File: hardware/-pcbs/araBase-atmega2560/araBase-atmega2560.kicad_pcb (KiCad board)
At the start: 2 copper layers, 21 parts, among them J1 UI, U1 ATmega2560-16AU, U2 5V->3.3V, Y1 16MHz

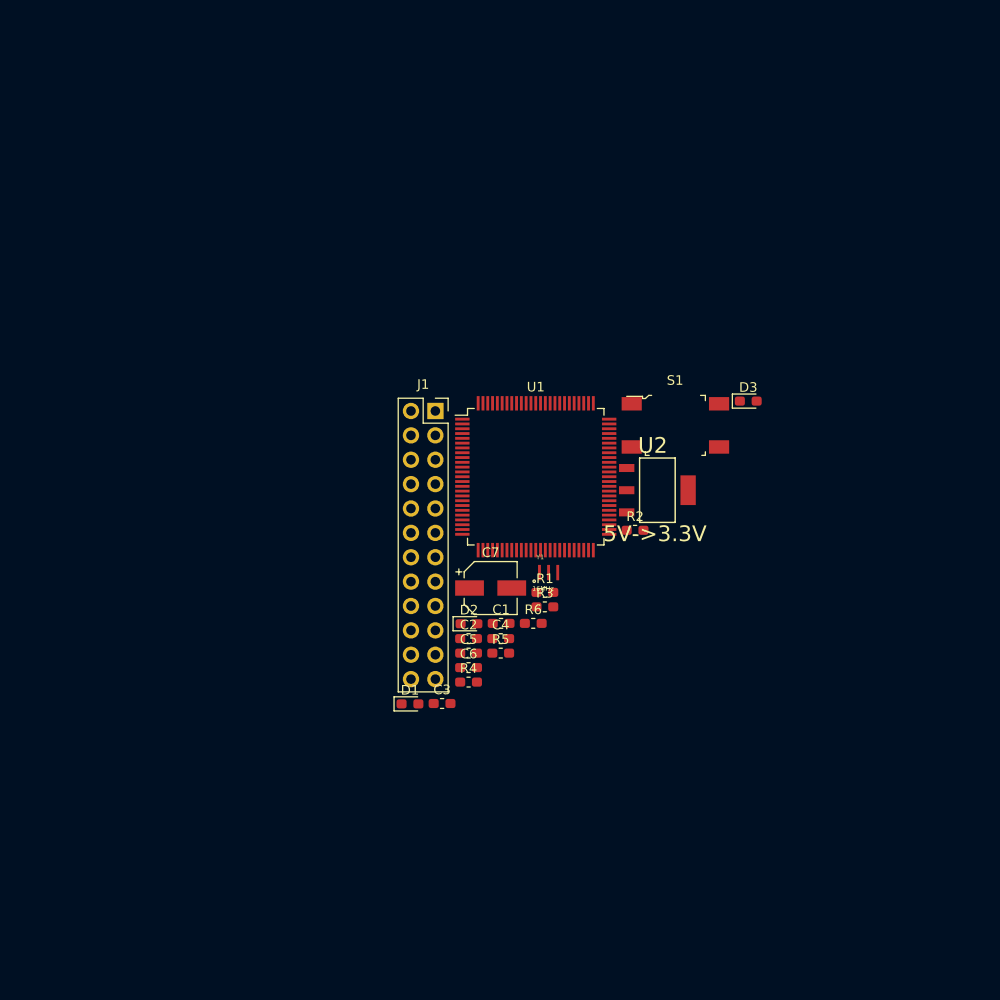
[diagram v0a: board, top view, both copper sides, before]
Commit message: Add 100mmx100mm edge cut and distribute footprints
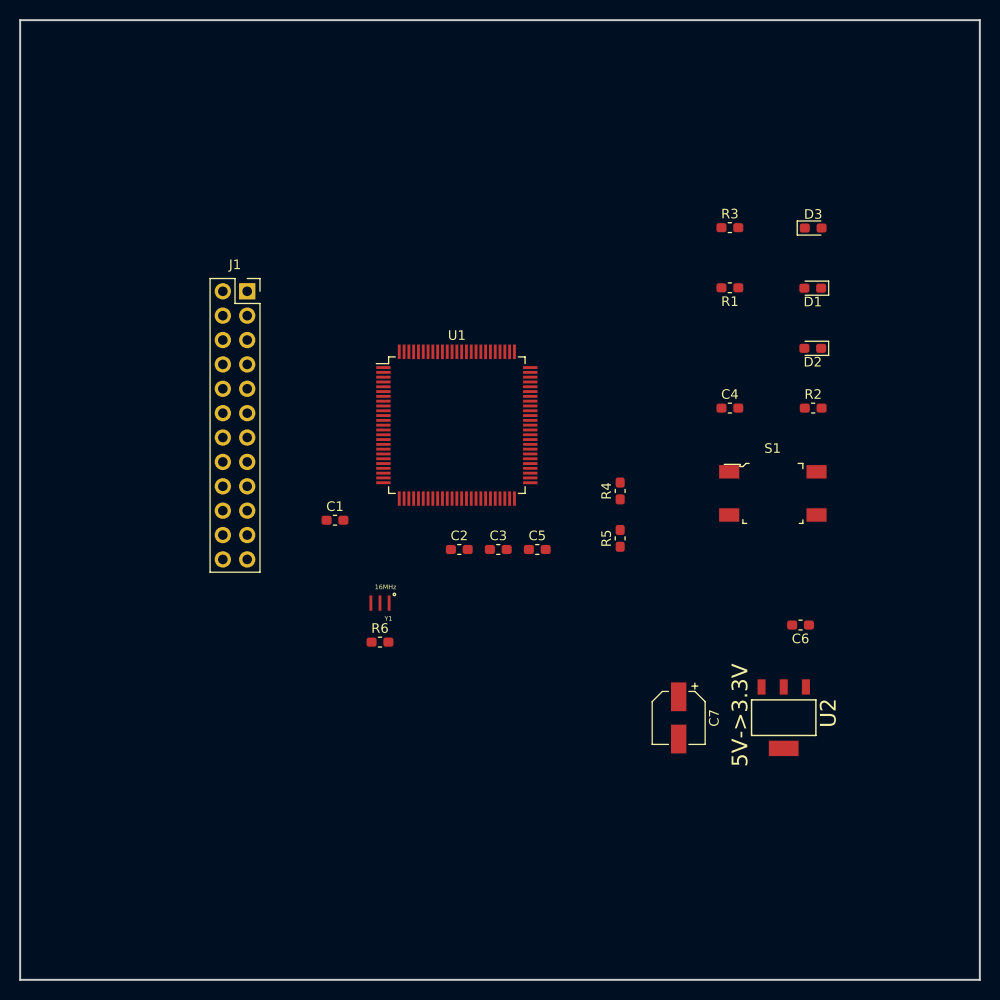
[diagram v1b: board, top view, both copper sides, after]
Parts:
- moved D1 60.3 mm to (132.6, 77.9), turned to 180 degrees
- moved D2 45.9 mm to (132.6, 84.2), turned to 180 degrees
- moved R3 44.0 mm to (124.0, 71.6)
- moved R1 37.1 mm to (124.0, 77.9), turned to 180 degrees
- moved C6 34.9 mm to (131.3, 113.0), turned to 180 degrees
- moved C4 33.9 mm to (124.0, 90.4)
- moved U2 27.1 mm to (129.6, 122.7), turned to 270 degrees
- moved R4 25.4 mm to (112.5, 99.1), turned to 90 degrees
- moved C7 23.8 mm to (118.6, 122.7), turned to 270 degrees
- moved J1 23.2 mm to (73.7, 78.3)
- moved R2 22.5 mm to (132.6, 90.4)
- moved C1 20.4 mm to (82.8, 102.1)
- moved D3 19.3 mm to (132.6, 71.7)
- moved Y1 17.9 mm to (87.5, 110.7), turned to 180 degrees
- moved R5 17.3 mm to (112.5, 104.0), turned to 90 degrees
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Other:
- board outline added: 100 x 100 mm

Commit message: Setup design rules for 10mil/10mil trace and 0.8mm/0.4mm via/drill
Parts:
- moved C2 3.09 mm to (92.7, 105.7), turned to 90 degrees
- moved C3 3.09 mm to (96.8, 105.7), turned to 90 degrees
- moved C5 3.09 mm to (100.8, 105.7), turned to 90 degrees
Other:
- net class Default: clearance 0.2 -> 0.254; trace_width 0.25 -> 0.254
- net class PWR added: clearance 0.3048, trace_width 0.3048, via_dia 0.8, via_drill 0.4
- rule trace_clearance: 0.2 -> 0.254
- rule trace_min: 0.2 -> 0.254
- rule via_min_drill: 0.3 -> 0.4
- rule via_min_size: 0.4 -> 0.8
